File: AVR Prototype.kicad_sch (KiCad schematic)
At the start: 22 parts

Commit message: Original V2 Update
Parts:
- removed FB1, FB2, FB3, FB4, FB5: (no value), symbol AVR-Prototype-rescue:Ferrite_Bead_Small-Device
- added C9: 10 uF, Capacitor_THT:C_Radial_D6.3mm_H11.0mm_P2.50mm, symbol Device:C_Polarized_US
- C1: renamed from C7; value (none) -> 10 pF; footprint (none) -> Capacitor_SMD:C_0805_2012Metric_Pad1.18x1.45mm_HandSolder; Mouser Part Number 80-C0805X220K3GAUTO -> 80-C0805C100K5RACAUTO
- C2: renamed from C8; value (none) -> 10 pF; footprint (none) -> Capacitor_SMD:C_0805_2012Metric_Pad1.18x1.45mm_HandSolder; Mouser Part Number 80-C0805X220K3GAUTO -> 80-C0805C100K5RACAUTO
- C3: renamed from C9; value (none) -> 0.1uF; footprint (none) -> Capacitor_SMD:C_0805_2012Metric_Pad1.18x1.45mm_HandSolder
- C4: renamed from C10; value (none) -> 0.1uF; footprint (none) -> Capacitor_SMD:C_0805_2012Metric_Pad1.18x1.45mm_HandSolder
- C5: renamed from C11; value (none) -> 0.1uF; footprint (none) -> Capacitor_SMD:C_0805_2012Metric_Pad1.18x1.45mm_HandSolder
- C6: renamed from C12; value (none) -> 0.1uF; footprint (none) -> Capacitor_SMD:C_0805_2012Metric_Pad1.18x1.45mm_HandSolder
- C7: renamed from C13; value (none) -> 0.1uF; footprint (none) -> Capacitor_SMD:C_0805_2012Metric_Pad1.18x1.45mm_HandSolder
- C8: renamed from C14; value (none) -> 0.1uF; footprint (none) -> Capacitor_SMD:C_0805_2012Metric_Pad1.18x1.45mm_HandSolder
- FB1: renamed from FB6; value (none) -> Fe; footprint (none) -> Resistor_SMD:R_0805_2012Metric_Pad1.20x1.40mm_HandSolder
- J1: renamed from J2; value (none) -> AVR-ISP; footprint (none) -> BRG_Footprints:AVR_ISP
- J2: renamed from J3; value (none) -> Aux; footprint (none) -> Connector_PinHeader_2.54mm:PinHeader_1x02_P2.54mm_Vertical
- J3: renamed from J4; value (none) -> Conn_01x06; footprint (none) -> Connector_PinHeader_2.54mm:PinHeader_1x06_P2.54mm_Vertical
- J4: renamed from J5; value (none) -> ConnA; footprint (none) -> Connector_PinHeader_2.54mm:PinHeader_1x24_P2.54mm_Vertical
- J5: renamed from J6; value (none) -> ConnB; footprint (none) -> Connector_PinHeader_2.54mm:PinHeader_1x24_P2.54mm_Vertical
- R1: renamed from R2; value (none) -> 10k; footprint (none) -> Resistor_SMD:R_0805_2012Metric_Pad1.20x1.40mm_HandSolder; Mouser Part Number 660-RK73H2ATTD1002F -> 667-ERJ-6GEYJ103V
- U1: value (none) -> ATxmega256A3U-AU; footprint (none) -> Package_QFP:TQFP-64_14x14mm_P0.8mm
- Y1: value (none) -> 16 MHz; footprint (none) -> Crystal:Crystal_HC49-U_Vertical
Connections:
- net +3V3: now also FB1.1, U1.15 (VCC), U1.25 (VCC), U1.35 (VCC), U1.45 (VCC), U1.53 (VCC); no longer C8.2, FB1.2
- net GND: now also C9.2
- net at U1.61 (AVCC): now also C8.2, FB1.2, C9.1; no longer FB1.1
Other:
- moved on the sheet: FB1

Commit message: Routed by FreeRouting
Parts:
- C9: Mouser Part Number 80-ESK106M100AE3EA -> 667-ECA-2AM100
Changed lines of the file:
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@@
   (junction (at 60.96 96.52) (diameter 0) (color 0 0 0 0)
   )
-  (junction (at 132.08 58.42) (diameter 0) (color 0 0 0 0)
-  )
   (junction (at 121.92 195.58) (diameter 0) (color 0 0 0 0)
   )
@@
   (junction (at 99.06 38.1) (diameter 0) (color 0 0 0 0)
   )
-  (junction (at 111.76 167.386) (diameter 0) (color 0 0 0 0)
-  )
-  (junction (at 127 58.42) (diameter 0) (color 0 0 0 0)
-  )
   (junction (at 111.76 38.1) (diameter 0) (color 0 0 0 0)
   )
@@
   (junction (at 127 168.91) (diameter 0) (color 0 0 0 0)
   )
-  (junction (at 121.92 58.166) (diameter 0) (color 0 0 0 0)
-  )
-  (junction (at 111.76 58.42) (diameter 0) (color 0 0 0 0)
-  )
   (junction (at 137.16 66.04) (diameter 0) (color 0 0 0 0)
-  )
-  (junction (at 121.92 167.64) (diameter 0) (color 0 0 0 0)
   )
   (junction (at 73.66 109.22) (diameter 0) (color 0 0 0 0)
@@
     (stroke (width 0) (type default) (color 0 0 0 0))
   )
-  (wire (pts (xy 121.92 167.64) (xy 121.92 190.5))
-    (stroke (width 0) (type default) (color 0 0 0 0))
-  )
   (wire (pts (xy 137.16 63.5) (xy 137.16 66.04))
     (stroke (width 0) (type default) (color 0 0 0 0))
@@
     (stroke (width 0) (type default) (color 0 0 0 0))
   )
-  (wire (pts (xy 127 58.42) (xy 132.08 58.42))
-    (stroke (width 0) (type default) (color 0 0 0 0))
-  )
   (wire (pts (xy 60.96 99.06) (xy 60.96 96.52))
     (stroke (width 0) (type default) (color 0 0 0 0))
   )
-  (wire (pts (xy 111.76 167.386) (xy 111.76 190.5))
-    (stroke (width 0) (type default) (color 0 0 0 0))
-  )
   (wire (pts (xy 78.74 124.46) (xy 66.04 124.46))
     (stroke (width 0) (type default) (color 0 0 0 0))
@@
     (stroke (width 0) (type default) (color 0 0 0 0))
   )
-  (wire (pts (xy 121.92 58.166) (xy 121.92 69.85))
+  (wire (pts (xy 121.92 45.72) (xy 121.92 69.85))
     (stroke (width 0) (type default) (color 0 0 0 0))
   )
@@
     (stroke (width 0) (type default) (color 0 0 0 0))
   )
-  (wire (pts (xy 111.76 163.83) (xy 111.76 167.386))
+  (wire (pts (xy 111.76 163.83) (xy 111.76 190.5))
     (stroke (width 0) (type default) (color 0 0 0 0))
   )
@@
     (stroke (width 0) (type default) (color 0 0 0 0))
   )
-  (wire (pts (xy 111.76 45.72) (xy 111.76 58.42))
+  (wire (pts (xy 111.76 45.72) (xy 111.76 69.85))
     (stroke (width 0) (type default) (color 0 0 0 0))
   )
@@
     (stroke (width 0) (type default) (color 0 0 0 0))
   )
-  (wire (pts (xy 124.46 58.42) (xy 127 58.42))
-    (stroke (width 0) (type default) (color 0 0 0 0))
-  )
   (wire (pts (xy 111.76 195.58) (xy 121.92 195.58))
     (stroke (width 0) (type default) (color 0 0 0 0))
@@
     (stroke (width 0) (type default) (color 0 0 0 0))
   )
-  (wire (pts (xy 121.92 45.72) (xy 121.92 58.166))
-    (stroke (width 0) (type default) (color 0 0 0 0))
-  )
   (wire (pts (xy 137.16 45.72) (xy 132.08 45.72))
     (stroke (width 0) (type default) (color 0 0 0 0))
   )
-  (wire (pts (xy 121.92 163.83) (xy 121.92 167.64))
+  (wire (pts (xy 121.92 163.83) (xy 121.92 190.5))
     (stroke (width 0) (type default) (color 0 0 0 0))
   )
@@
     (stroke (width 0) (type default) (color 0 0 0 0))
   )
-  (wire (pts (xy 132.08 58.42) (xy 132.08 69.85))
-    (stroke (width 0) (type default) (color 0 0 0 0))
-  )
   (wire (pts (xy 121.92 38.1) (xy 132.08 38.1))
     (stroke (width 0) (type default) (color 0 0 0 0))
@@
     (stroke (width 0) (type default) (color 0 0 0 0))
   )
-  (wire (pts (xy 111.76 58.42) (xy 111.76 69.85))
-    (stroke (width 0) (type default) (color 0 0 0 0))
-  )
   (wire (pts (xy 111.76 190.5) (xy 111.76 195.58))
     (stroke (width 0) (type default) (color 0 0 0 0))
@@
     (stroke (width 0) (type default) (color 0 0 0 0))
   )
-  (wire (pts (xy 132.08 45.72) (xy 132.08 58.42))
+  (wire (pts (xy 132.08 45.72) (xy 132.08 69.85))
     (stroke (width 0) (type default) (color 0 0 0 0))
   )
@@
     (pin "1")
   )
-  (symbol (lib_id "power:PWR_FLAG") (at 111.76 167.386 90) (unit 1)
-    (in_bom yes) (on_board yes)
-    (property "Reference" "#FLG02" (id 0) (at 109.855 167.386 0)
-      (effects (font (size 1.27 1.27)) hide)
-    )
-    (property "Value" "PWR_FLAG" (id 1) (at 116.586 165.608 90)
-      (effects (font (size 1.27 1.27)) (justify left))
-    )
-    (property "Footprint" "" (id 2) (at 111.76 167.386 0)
-      (effects (font (size 1.27 1.27)) hide)
-    )
-    (property "Datasheet" "~" (id 3) (at 111.76 167.386 0)
-      (effects (font (size 1.27 1.27)) hide)
-    )
-    (pin "1")
-  )
-  (symbol (lib_id "power:PWR_FLAG") (at 121.92 167.64 90) (unit 1)
-    (in_bom yes) (on_board yes)
-    (property "Reference" "#FLG04" (id 0) (at 120.015 167.64 0)
-      (effects (font (size 1.27 1.27)) hide)
-    )
-    (property "Value" "PWR_FLAG" (id 1) (at 126.746 165.862 90)
-      (effects (font (size 1.27 1.27)) (justify left))
-    )
-    (property "Footprint" "" (id 2) (at 121.92 167.64 0)
-      (effects (font (size 1.27 1.27)) hide)
-    )
-    (property "Datasheet" "~" (id 3) (at 121.92 167.64 0)
-      (effects (font (size 1.27 1.27)) hide)
-    )
-    (pin "1")
-  )
   (symbol (lib_id "power:PWR_FLAG") (at 132.08 167.64 90) (unit 1)
     (in_bom yes) (on_board yes)
@@
     )
     (property "Datasheet" "" (id 3) (at 152.4 68.58 0)
-      (effects (font (size 1.27 1.27)) hide)
-    )
-    (pin "1")
-  )
-  (symbol (lib_id "power:PWR_FLAG") (at 111.76 58.42 90) (unit 1)
-    (in_bom yes) (on_board yes)
-    (property "Reference" "#FLG01" (id 0) (at 109.855 58.42 0)
-      (effects (font (size 1.27 1.27)) hide)
-    )
-    (property "Value" "PWR_FLAG" (id 1) (at 116.586 56.388 90)
-      (effects (font (size 1.27 1.27)) (justify left))
-    )
-    (property "Footprint" "" (id 2) (at 111.76 58.42 0)
-      (effects (font (size 1.27 1.27)) hide)
-    )
-    (property "Datasheet" "~" (id 3) (at 111.76 58.42 0)
-      (effects (font (size 1.27 1.27)) hide)
-    )
-    (pin "1")
-  )
-  (symbol (lib_id "power:PWR_FLAG") (at 121.92 58.166 90) (unit 1)
-    (in_bom yes) (on_board yes)
-    (property "Reference" "#FLG03" (id 0) (at 120.015 58.166 0)
-      (effects (font (size 1.27 1.27)) hide)
-    )
-    (property "Value" "PWR_FLAG" (id 1) (at 126.746 56.388 90)
-      (effects (font (size 1.27 1.27)) (justify left))
-    )
-    (property "Footprint" "" (id 2) (at 121.92 58.166 0)
-      (effects (font (size 1.27 1.27)) hide)
-    )
-    (property "Datasheet" "~" (id 3) (at 121.92 58.166 0)
-      (effects (font (size 1.27 1.27)) hide)
-    )
-    (pin "1")
-  )
-  (symbol (lib_id "power:PWR_FLAG") (at 132.08 58.42 90) (unit 1)
-    (in_bom yes) (on_board yes)
-    (property "Reference" "#FLG05" (id 0) (at 130.175 58.42 0)
-      (effects (font (size 1.27 1.27)) hide)
-    )
-    (property "Value" "PWR_FLAG" (id 1) (at 137.16 56.388 90)
-      (effects (font (size 1.27 1.27)) (justify left))
-    )
-    (property "Footprint" "" (id 2) (at 132.08 58.42 0)
-      (effects (font (size 1.27 1.27)) hide)
-    )
-    (property "Datasheet" "~" (id 3) (at 132.08 58.42 0)
       (effects (font (size 1.27 1.27)) hide)
     )
@@
       (effects (font (size 1.27 1.27)) hide)
     )
-    (property "Mouser Part Number" "80-ESK106M100AE3EA" (id 4) (at 140.97 190.5 0)
+    (property "Mouser Part Number" "667-ECA-2AM100" (id 4) (at 140.97 190.5 0)
       (effects (font (size 1.27 1.27)) hide)
     )
@@
   )
   (symbol_instances
-    (path "/00000000-0000-0000-0000-00005fc6daf7"
-      (reference "#FLG01") (unit 1) (value "PWR_FLAG") (footprint "")
-    )
-    (path "/00000000-0000-0000-0000-00005fbe15ea"
-      (reference "#FLG02") (unit 1) (value "PWR_FLAG") (footprint "")
-    )
-    (path "/00000000-0000-0000-0000-00005fc6f1d8"
-      (reference "#FLG03") (unit 1) (value "PWR_FLAG") (footprint "")
-    )
-    (path "/00000000-0000-0000-0000-00005fbe21e2"
-      (reference "#FLG04") (unit 1) (value "PWR_FLAG") (footprint "")
-    )
-    (path "/00000000-0000-0000-0000-00005fc6f792"
-      (reference "#FLG05") (unit 1) (value "PWR_FLAG") (footprint "")
-    )
     (path "/00000000-0000-0000-0000-00005fbe2742"
       (reference "#FLG06") (unit 1) (value "PWR_FLAG") (footprint "")
@@
     )
     (path "/00000000-0000-0000-0000-00005fb56876/00000000-0000-0000-0000-00005fb2faf8"
-      (reference "C10") (unit 1) (value "10 uF") (footprint "Capacitor_THT:C_Rect_L13.5mm_W5.0mm_P10.00mm_FKS3_FKP3_MKS4")
+      (reference "C10") (unit 1) (value "10 uF") (footprint "Capacitor_SMD:C_2220_5650Metric_Pad1.97x5.40mm_HandSolder")
     )
     (path "/00000000-0000-0000-0000-00005fb56876/00000000-0000-0000-0000-00005fb4318d"
-      (reference "C11") (unit 1) (value "10 uF") (footprint "Capacitor_THT:C_Rect_L13.5mm_W5.0mm_P10.00mm_FKS3_FKP3_MKS4")
+      (reference "C11") (unit 1) (value "10 uF") (footprint "Capacitor_SMD:C_2220_5650Metric_Pad1.97x5.40mm_HandSolder")
     )
     (path "/00000000-0000-0000-0000-00005fb56876/00000000-0000-0000-0000-00005fb3098b"

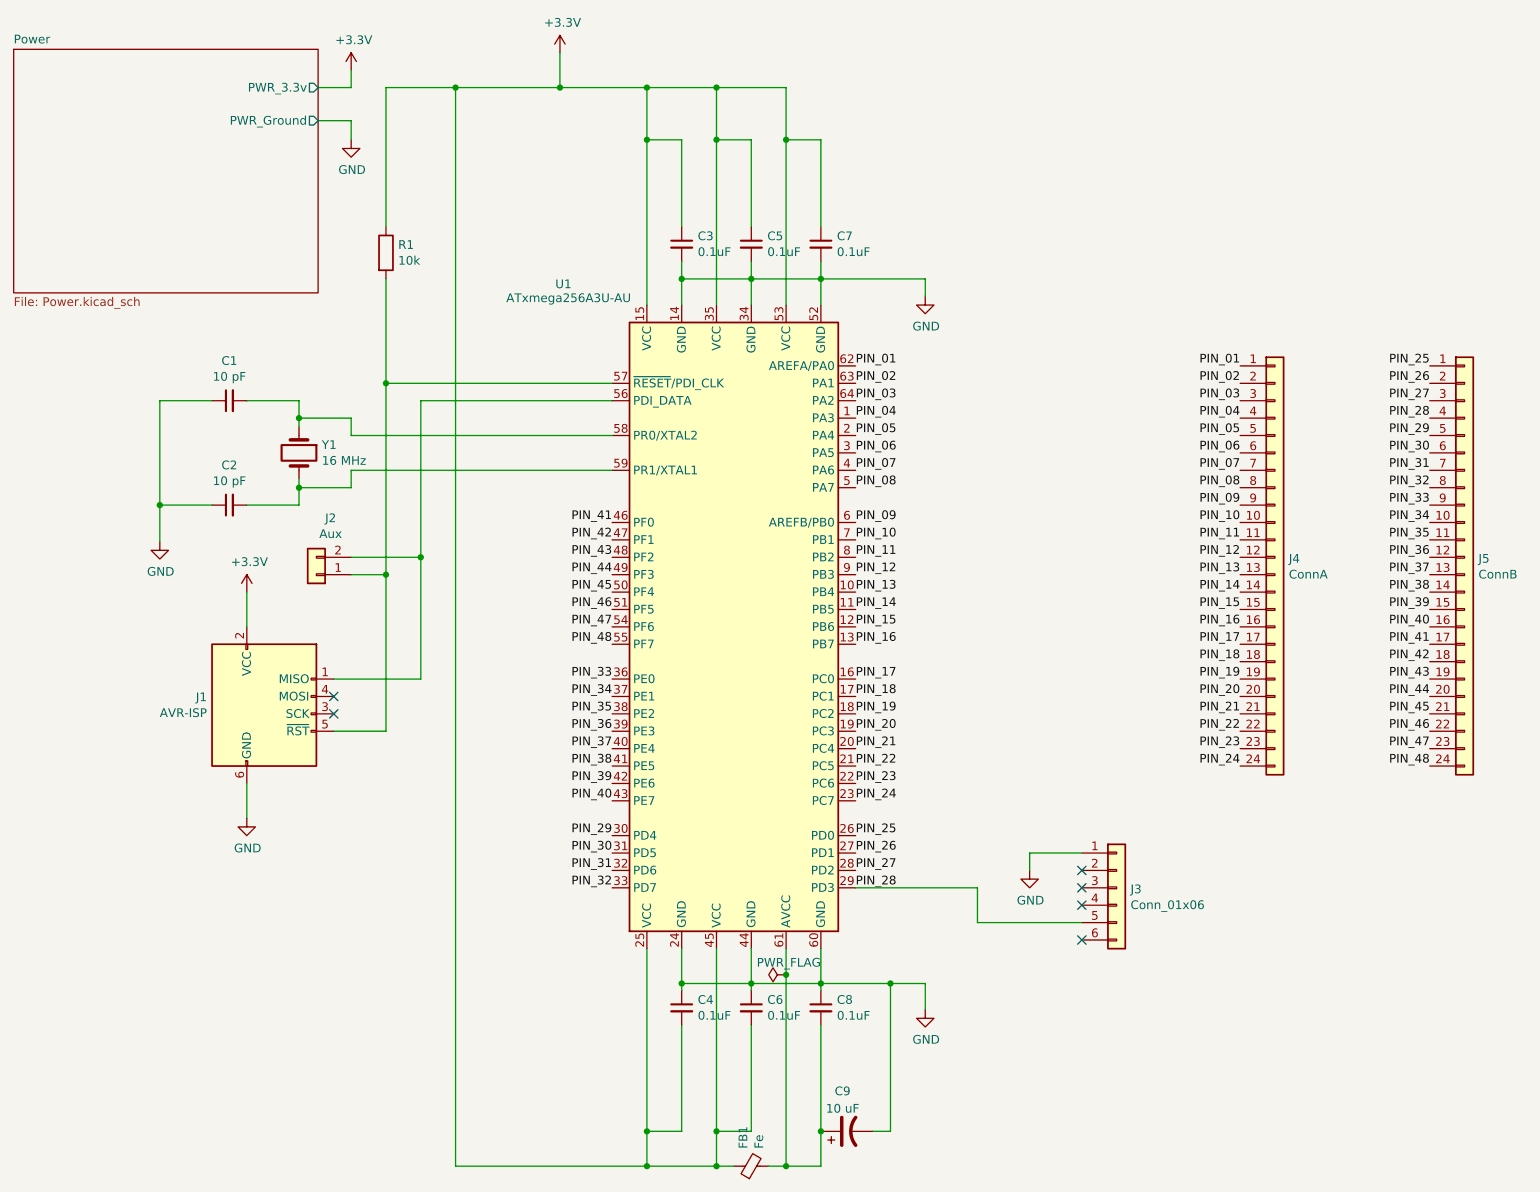
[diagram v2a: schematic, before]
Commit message: Updated V3.3 Converter to VCC input
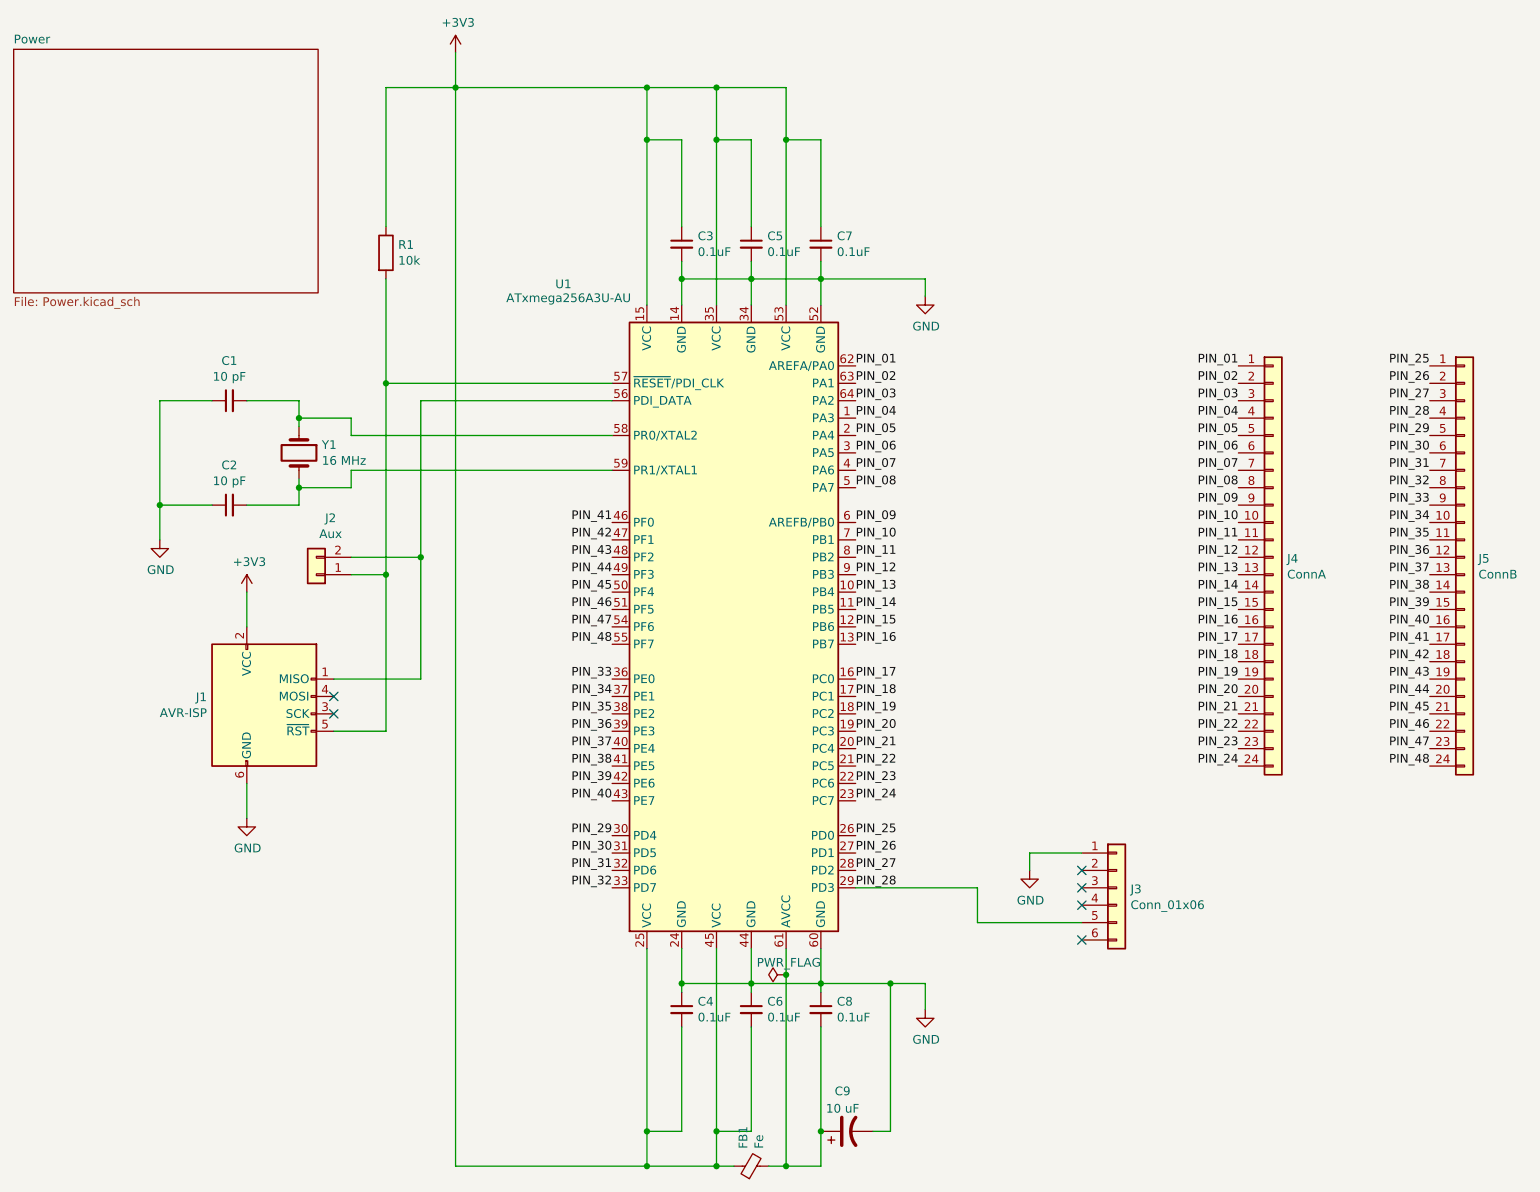
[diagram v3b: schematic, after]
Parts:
- C1, C2: Manufacturer_Part_Number C0805X220K3GACAUTO -> A001
- C3, C4, C5, C6, C7, C8: Manufacturer_Part_Number C0805C104J5RAUTO -> A002
- C9: footprint Capacitor_THT:C_Radial_D6.3mm_H11.0mm_P2.50mm -> Capacitor_THT:C_Radial_D5.0mm_H11.0mm_P2.00mm; Manufacturer_Part_Number (none) -> B102
- FB1: Manufacturer_Part_Number BK2125HS101-T -> A005
- J1: Manufacturer_Part_Number 1465 -> B105
- J2: Manufacturer_Part_Number (none) -> B110
- J3: Manufacturer_Part_Number (none) -> B107
- J4, J5: Manufacturer_Part_Number (none) -> B106
- R1: Manufacturer_Part_Number RK73H2ATTD1002F -> A008
- U1: Manufacturer_Part_Number ATXMEGA256A3U-AU -> C201
- Y1: Manufacturer_Part_Number ABL-16.000MHZB1U -> B115
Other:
- sheet Power ports: added none; removed PWR_3.3v, PWR_Ground
